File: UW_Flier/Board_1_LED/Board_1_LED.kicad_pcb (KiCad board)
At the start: 2 copper layers, 11 parts, among them J1 RESET, J2 SWDIO, J3 SWDCLK, J4 GND, J5 VDD, J6 LED_DRAIN, Q1 CSD13385F5, U1 EYSHSNZWZ_module_stub

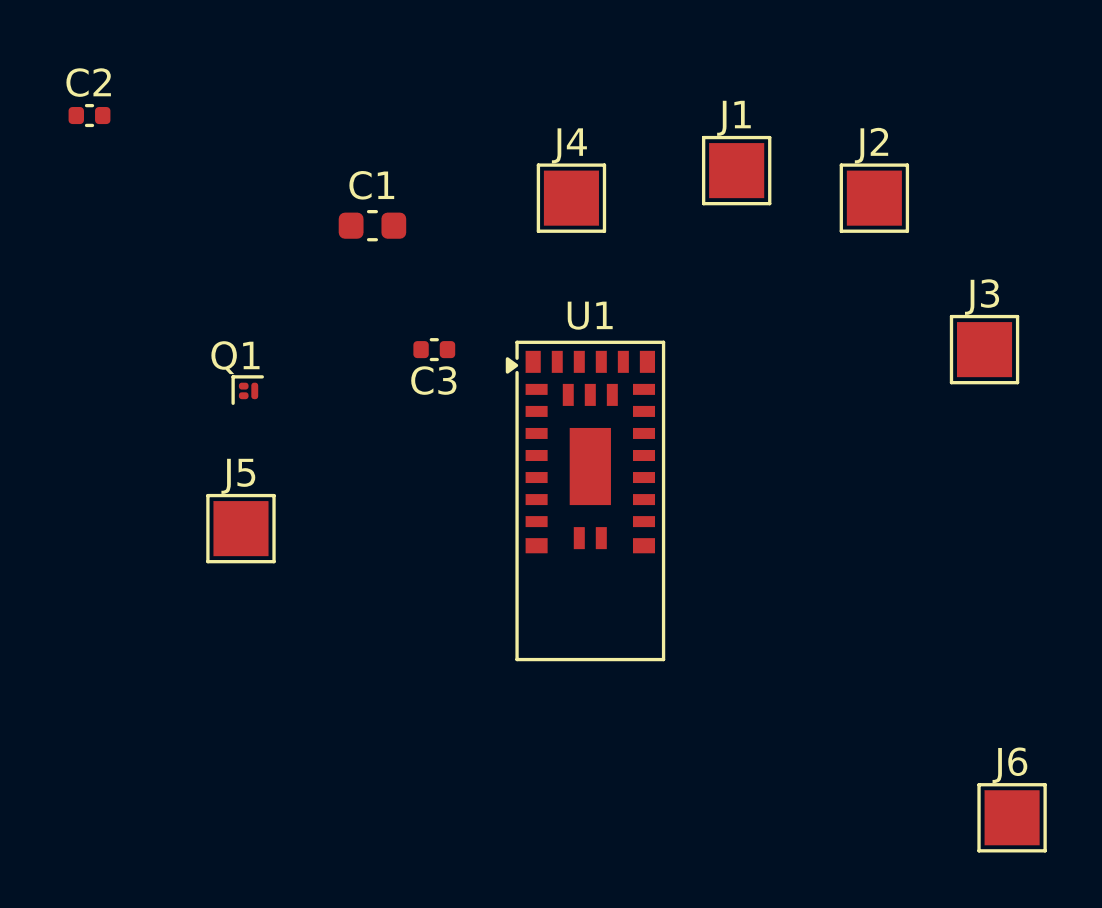
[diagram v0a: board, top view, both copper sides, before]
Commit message: first iteration of PCB 1 (testing with mosfet / LED)
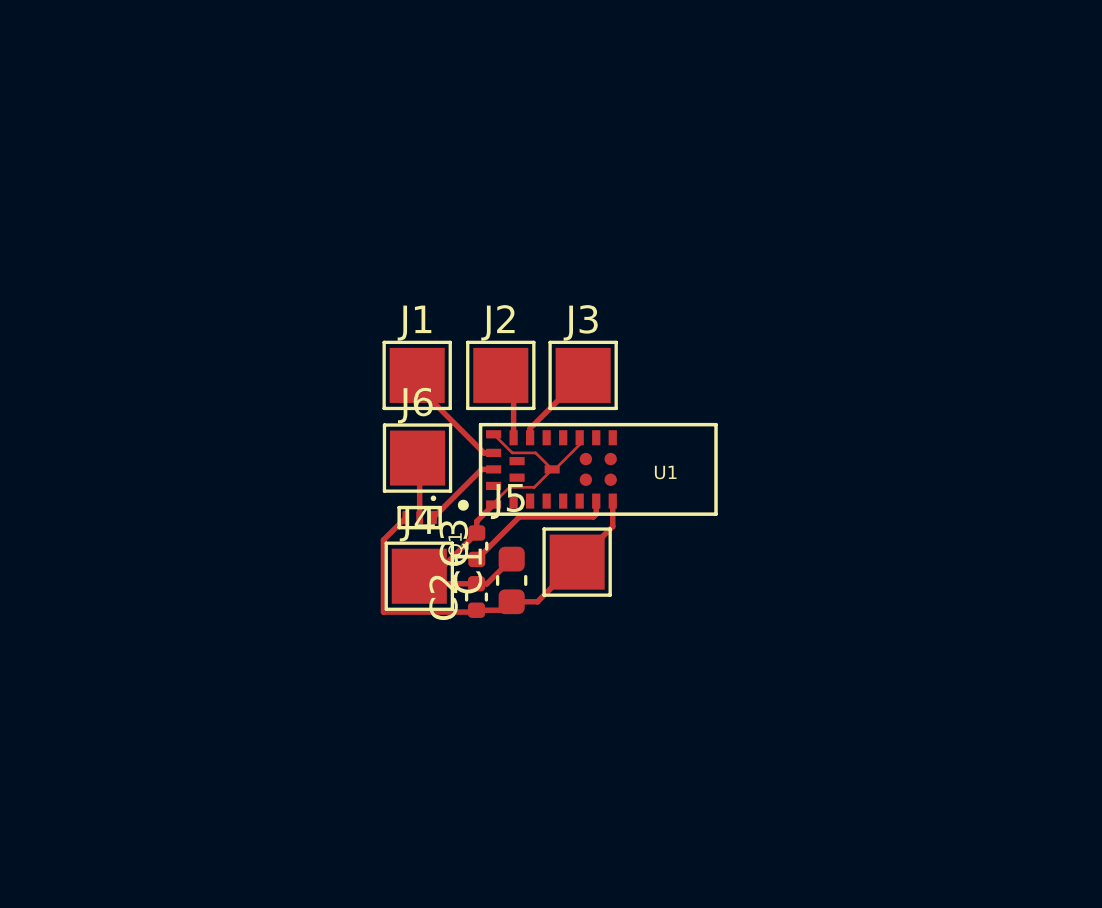
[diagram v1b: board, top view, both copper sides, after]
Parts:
- Q1: footprint Package_DFN_QFN:Texas_PicoStar_DFN-3_0.69x0.60mm -> CSD13385F5:TRANS_CSD13385F5
- U1: footprint RF_Module:Taiyo-Yuden_EYSGJNZWY -> EYSHSNZWZ:XCVR_EYSHSNZWZ
- moved J6 25.2 mm to (102.4, 73.9)
- moved C2 22.4 mm to (104.6, 79.0), turned to 90 degrees
- moved J2 15.0 mm to (105.4, 70.9)
- moved J4 14.8 mm to (102.5, 78.2)
- moved J3 14.6 mm to (108.4, 70.9)
- moved C1 13.8 mm to (105.8, 78.4), turned to 90 degrees
- moved J1 13.8 mm to (102.4, 70.9)
- moved J5 12.3 mm to (108.2, 77.7)
- moved Q1 7.73 mm to (102.5, 76.1), turned to -90 degrees
- moved C3 7.30 mm to (104.6, 77.1), turned to 90 degrees
- moved U1 1.18 mm to (109.0, 74.3)
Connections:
- U1 pad 2: Net-(Q1-G) -> unconnected-(U1-P0.06-Pad2)
- U1 pad 20: unconnected-(U1-P0.08-Pad20) -> Net-(Q1-G)
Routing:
- net Net-(J4-Pin_1): track 0.00 -> 14.8 mm
- net Net-(J5-Pin_1): track 0.00 -> 14.3 mm
- net Net-(U1-DEC4): track 0.00 -> 5.49 mm
- net Net-(J1-Pin_1): track 0.00 -> 4.19 mm
- net Net-(J3-Pin_1): track 0.00 -> 3.06 mm
- net Net-(Q1-G): track 0.00 -> 2.91 mm
- net Net-(J2-Pin_1): track 0.00 -> 2.46 mm
- net Net-(J6-Pin_1): track 0.00 -> 2.19 mm
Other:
- board text added: "${REFERENCE}"
